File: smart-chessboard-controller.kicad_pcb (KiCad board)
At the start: 4 copper layers, 89.8 x 50.9 mm, 65 parts, among them J1 USB_C_Receptacle_USB2.0, J2 Micro_SD_Card_Det_Hirose_DM3C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, J3 Conn_02x03_Odd_Even, J4 Conn_01x12_MountingPin, J5 NX3224T024, J8 Conn_01x05, J9 Conn_01x05, Q1 S8050, Q2 S8050, SW2 SW_SPST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

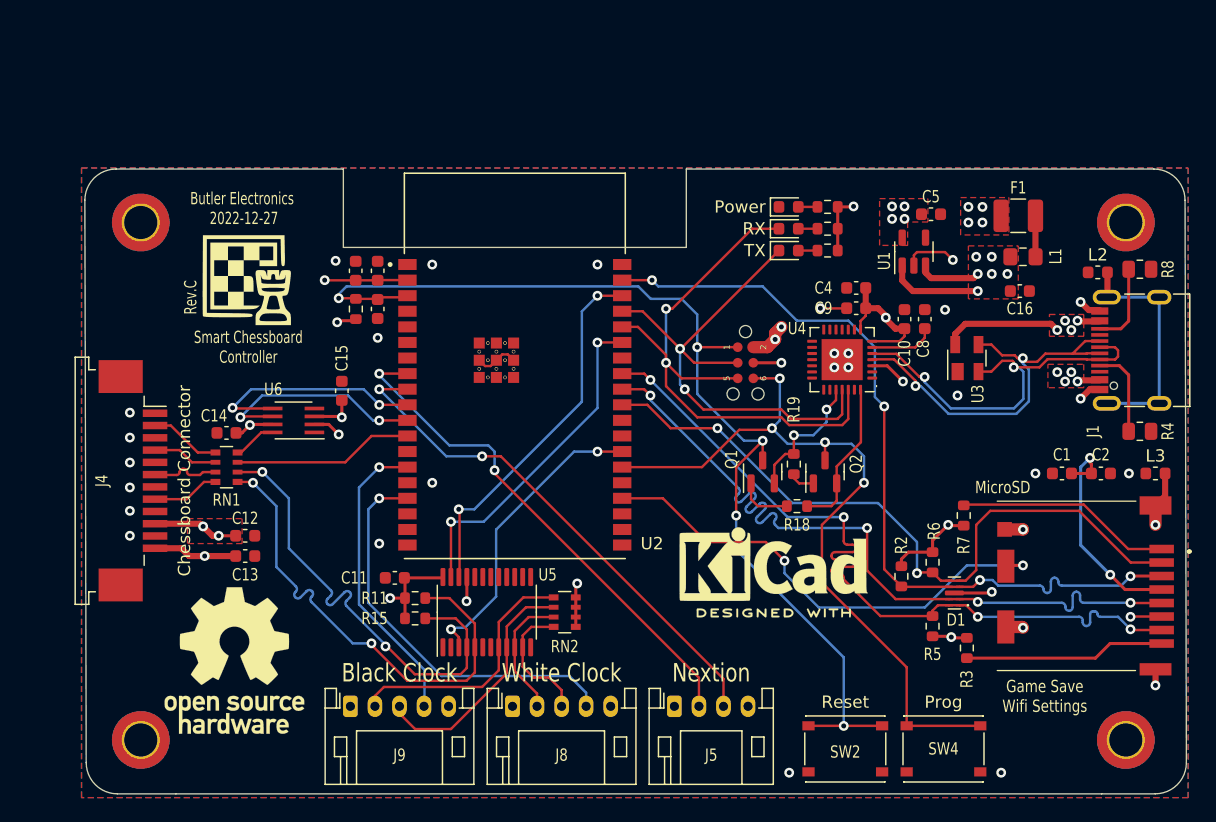
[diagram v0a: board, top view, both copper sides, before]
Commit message: refactor schematic/pcb to add/remove components
- remove ESP programmer Tag Connect interface
- replace set of resistors to resistor array for SD card
- add pull-up resistors for interrupt and bus buffer enable pin
- tune trace length matching for data lines (i2c, ttl and spi)
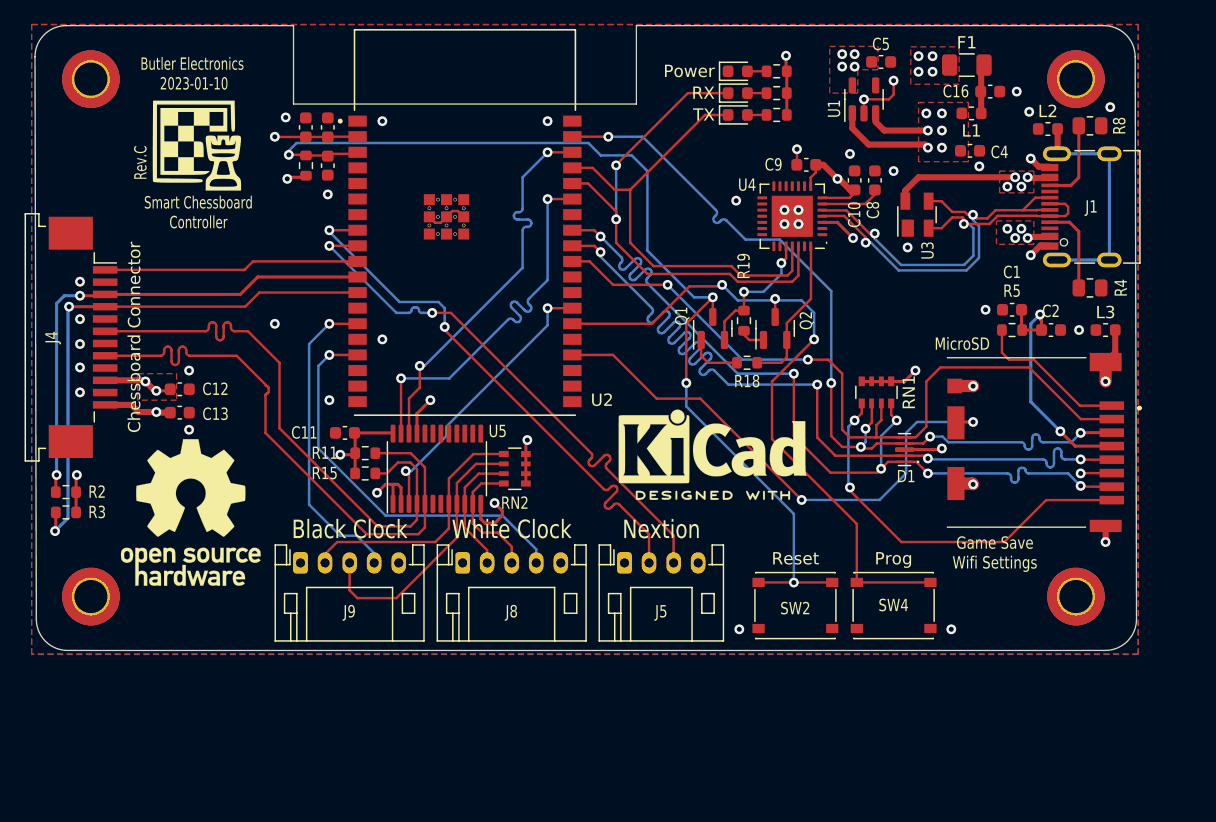
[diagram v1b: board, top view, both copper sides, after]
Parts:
- removed C14, C15: 100nF, Capacitor_SMD:C_0603_1608Metric
- removed J3: Conn_02x03_Odd_Even, Tag_Connect:TC2030-IDC-NL
- removed R6, R7: 47K, Resistor_SMD:R_0603_1608Metric
- removed U6: TXS0102DCT, Package_SO:SSOP-8_2.95x2.8mm_P0.65mm
- F1: value C207047 -> BHFUSE BSMD1206-200-12V; footprint Fuse:Fuse_1210_3225Metric -> Fuse:Fuse_1206_3216Metric
- L1: footprint Inductor_SMD:L_0805_2012Metric_Pad1.15x1.40mm_HandSolder -> Inductor_SMD:L_0603_1608Metric
- R14: value 470 -> 1K
- R2, R3, R5: value 47K -> 10K
- RN1: value 0 -> 10K
- moved R3 74.2 mm to (72.1, 81.3), turned to 180 degrees
- moved R2 68.4 mm to (72.1, 79.6), turned to 180 degrees
- moved RN1 53.3 mm to (138.2, 71.5), turned to 90 degrees
- moved R5 25.0 mm to (149.2, 66.4), turned to 0 degrees
- moved C16 16.4 mm to (147.4, 47.0)
- moved C4 14.5 mm to (145.8, 51.8), turned to 180 degrees
- moved C1 13.9 mm to (149.2, 64.8)
- moved C12 13.1 mm to (81.4, 71.2)
- moved C5 13.1 mm to (138.6, 44.6)
- moved U1 13.1 mm to (137.2, 47.6)
- moved F1 13.0 mm to (145.5, 44.8)
- moved C13 12.8 mm to (81.4, 73.2)
- moved REF** 12.6 mm to (82.3, 81.3)
- moved C11 12.5 mm to (94.9, 74.8)
- moved R11 12.5 mm to (96.5, 76.5)
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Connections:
- C16 pad 2: 5V -> Net-(F1-Pad2)
- J2 pad 8: Net-(J2-Pad8) -> Net-(RN1-Pad1)
- J4 pad 1: GND -> /LED_IC
- J4 pad 2: Net-(J4-Pad2) -> GND
- J4 pad 3: GND -> /~{BUF_EN}
- J4 pad 4: Net-(J4-Pad4) -> /~{IO_INT}
- J4 pad 6: Net-(J4-Pad6) -> ~{SDA_IOMUX}
- J4 pad 8: Net-(J4-Pad8) -> ~{SCL_IOMUX}
- R2 pad 1: /SD_MOSI -> 3V3
- R2 pad 2: 3V3 -> /~{BUF_EN}
- R3 pad 1: Net-(J2-Pad8) -> 3V3
- R3 pad 2: 3V3 -> /~{IO_INT}
- R5 pad 1: /SD_MISO -> Net-(J2-Pad1)
- RN1 pad 1: Net-(J4-Pad2) -> Net-(RN1-Pad1)
- RN1 pad 2: Net-(J4-Pad4) -> /SD_MOSI
- RN1 pad 3: Net-(J4-Pad6) -> /SD_SS
- RN1 pad 4: Net-(J4-Pad8) -> /SD_MISO
- RN1 pad 5: ~{SCL_IOMUX} -> 3V3
- RN1 pad 6: ~{SDA_IOMUX} -> 3V3
- RN1 pad 7: /IO_INT -> 3V3
- RN1 pad 8: /LED_IC_5 -> 3V3
- U2 pad 10: /LED_IC_3 -> /LED_IC
- U2 pad 11: /VLS_EN -> /~{BUF_EN}
- U2 pad 12: /IO_INT -> /~{IO_INT}
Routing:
- net /~{IO_INT}: track 0.00 -> 44.3 mm, vias 0 -> 2
- net /~{BUF_EN}: track 0.00 -> 40.8 mm, vias 0 -> 2
- net Net-(RN1-Pad1): track 0.00 -> 32.1 mm, vias 0 -> 2
- net VBUS: track 58.0 -> 30.4 mm, vias 14 -> 12
- net /LED_IC: track 0.00 -> 20.9 mm
- net /LED_IC_3: track 18.7 -> 0.00 mm, vias 2 -> 0
- net /VLS_EN: track 17.8 -> 0.00 mm, vias 2 -> 0
- net 5V: track 137.2 -> 120.3 mm, vias 10 -> 9
- net Net-(J2-Pad8): track 16.4 -> 0.00 mm
- net 3V3: track 302.3 -> 286.0 mm, vias 15 -> 14
- net /IO_INT: track 14.7 -> 0.00 mm
- net /SD_SCK: track 62.8 -> 71.9 mm
- net ~{SDA_IOMUX}: track 37.7 -> 46.7 mm, vias 2 -> 0
- net ~{SCL_IOMUX}: track 39.5 -> 47.7 mm, vias 2 -> 0
- net /ESP_RX: track 48.5 -> 41.8 mm
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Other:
- board text added: "JLCJLCJLCJLCJLCJLC"

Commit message: update manufacturing files
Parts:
- U2: value ESP32-WROVER-32E -> ESP32-WROVER-E-N8R8
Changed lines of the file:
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@@
   (net 9 "/SD_SS")
   (net 10 "VBUS")
-  (net 11 "Net-(F1-Pad2)")
+  (net 11 "Net-(C16-Pad2)")
   (net 12 "/D_P")
   (net 13 "/D_N")
@@
   (net 38 "unconnected-(U2-Pad5)")
   (net 39 "/~{IO_INT}")
-  (net 40 "Net-(RN1-Pad1)")
+  (net 40 "Net-(J2-Pad8)")
   (net 41 "unconnected-(U2-Pad17)")
   (net 42 "unconnected-(U2-Pad18)")
@@
     (descr "Inductor SMD 0603 (1608 Metric), square (rectangular) end terminal, IPC_7351 nominal, (Body size source: http://www.tortai-tech.com/upload/download/2011102023233369053.pdf), generated with kicad-footprint-generator")
     (tags "inductor")
-    (property "LCSC" "C113018")
+    (property "LCSC" "C62708")
     (property "MFR_PART_NBR" "")
     (property "Sheetfile" "File: smart-chessboard-controller.kicad_sch")
@@
   (footprint "User Custom Footprint:XCVR_ESP32-WROVER-E-N4R8" (layer "F.Cu")
     (at 104.646 57.658)
-    (property "LCSC" " C2973667")
+    (property "LCSC" "C701348")
     (property "MANUFACTURER" "Espressif Systems")
     (property "MAXIMUM_PACKAGE_HEIGHT" "3.45 mm")
@@
       (effects (font (size 1 1) (thickness 0.15)))
     )
-    (fp_text value "ESP32-WROVER-32E" (at 6.24 18.515) (layer "F.Fab")
+    (fp_text value "ESP32-WROVER-E-N8R8" (at 6.24 18.515) (layer "F.Fab")
       (effects (font (size 1 1) (thickness 0.15)))
     )
@@
       (net 6 "/SD_MISO") (pinfunction "DAT0") (pintype "bidirectional"))
     (pad "8" smd rect (at -4.5 6.35 90) (size 0.7 2) (layers "F.Cu" "F.Paste" "F.Mask")
-      (net 40 "Net-(RN1-Pad1)") (pinfunction "DAT1") (pintype "bidirectional"))
+      (net 40 "Net-(J2-Pad8)") (pinfunction "DAT1") (pintype "bidirectional"))
     (pad "9" smd rect (at 1.8 -6.35 90) (size 2.7 1.4) (layers "F.Cu" "F.Paste" "F.Mask")
       (net 17 "/SD_DET") (pinfunction "DET_B") (pintype "passive"))
@@
     (fp_line (start 0.8 0.4) (end -0.8 0.4) (layer "F.Fab") (width 0.1))
     (pad "1" smd roundrect (at -0.7875 0 180) (size 0.875 0.95) (layers "F.Cu" "F.Paste" "F.Mask") (roundrect_rratio 0.25)
-      (net 11 "Net-(F1-Pad2)") (pintype "passive"))
+      (net 11 "Net-(C16-Pad2)") (pintype "passive"))
     (pad "2" smd roundrect (at 0.7875 0 180) (size 0.875 0.95) (layers "F.Cu" "F.Paste" "F.Mask") (roundrect_rratio 0.25)
       (net 4 "5V") (pintype "passive"))
@@
     (fp_line (start -0.8 1.6) (end -0.8 -1.6) (layer "F.Fab") (width 0.1))
     (pad "1" smd rect (at -0.9 -1.2 90) (size 0.8 0.5) (layers "F.Cu" "F.Paste" "F.Mask")
-      (net 40 "Net-(RN1-Pad1)") (pinfunction "R1.1") (pintype "passive"))
+      (net 40 "Net-(J2-Pad8)") (pinfunction "R1.1") (pintype "passive"))
     (pad "2" smd rect (at -0.9 -0.4 90) (size 0.8 0.4) (layers "F.Cu" "F.Paste" "F.Mask")
       (net 8 "/SD_MOSI") (pinfunction "R2.1") (pintype "passive"))
@@
       (net 2 "GND") (pintype "passive"))
     (pad "2" smd roundrect (at 0.775 0 180) (size 0.9 0.95) (layers "F.Cu" "F.Paste" "F.Mask") (roundrect_rratio 0.25)
-      (net 11 "Net-(F1-Pad2)") (pintype "passive"))
+      (net 11 "Net-(C16-Pad2)") (pintype "passive"))
     (model "${KICAD6_3DMODEL_DIR}/Capacitor_SMD.3dshapes/C_0603_1608Metric.wrl"
       (offset (xyz 0 0 0))
@@
       (net 10 "VBUS") (pintype "passive"))
     (pad "2" smd roundrect (at 1.4 0) (size 1.25 1.75) (layers "F.Cu" "F.Paste" "F.Mask") (roundrect_rratio 0.2)
-      (net 11 "Net-(F1-Pad2)") (pintype "passive"))
+      (net 11 "Net-(C16-Pad2)") (pintype "passive"))
     (model "${KICAD6_3DMODEL_DIR}/Fuse.3dshapes/Fuse_1206_3216Metric.wrl"
       (offset (xyz 0 0 0))
@@
     (descr "Inductor SMD 0603 (1608 Metric), square (rectangular) end terminal, IPC_7351 nominal, (Body size source: http://www.tortai-tech.com/upload/download/2011102023233369053.pdf), generated with kicad-footprint-generator")
     (tags "inductor")
-    (property "LCSC" "C113018")
+    (property "LCSC" "C62708")
     (property "MFR_PART_NBR" "")
     (property "Sheetfile" "File: smart-chessboard-controller.kicad_sch")

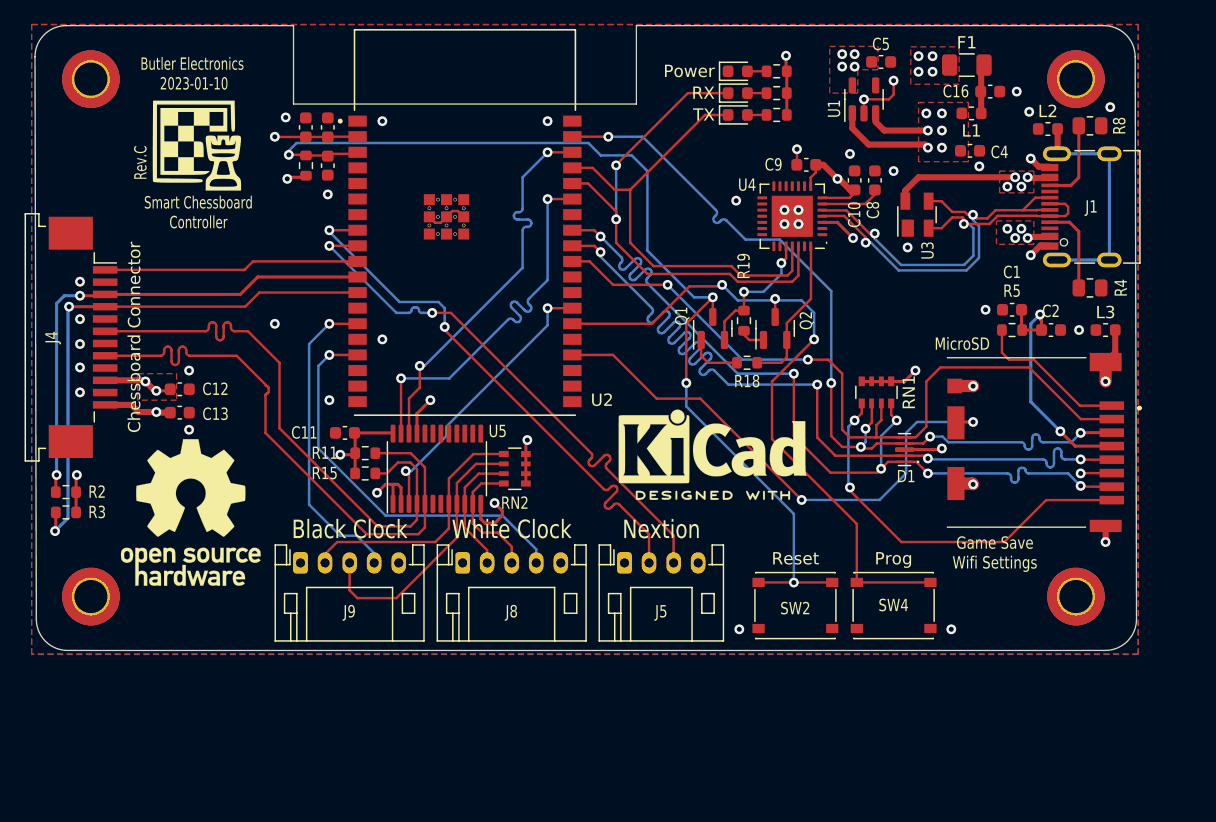
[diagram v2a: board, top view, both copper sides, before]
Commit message: update SD card detect pin assignment
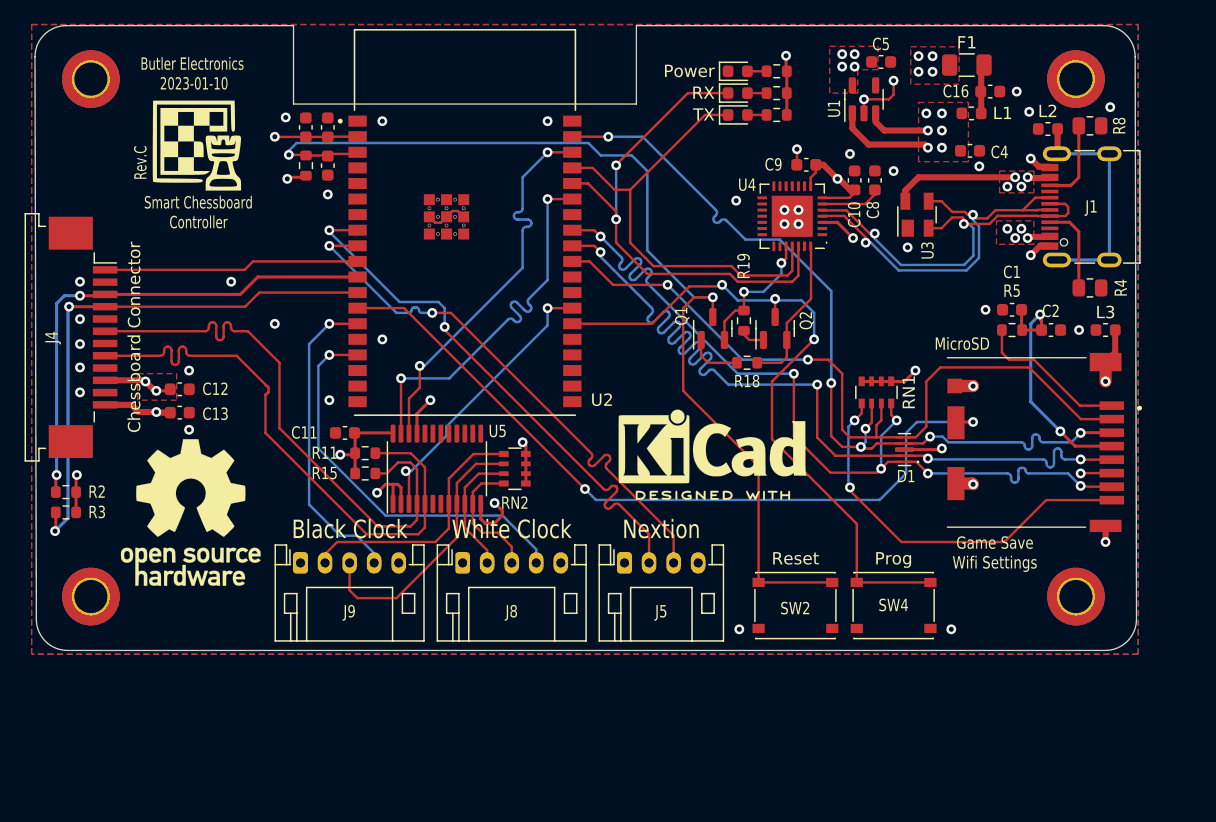
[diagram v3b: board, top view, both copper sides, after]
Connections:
- U2 pad 13: unconnected-(U2-Pad13) -> /SD_DET
- U2 pad 23: /SD_DET -> unconnected-(U2-Pad23)
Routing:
- net /SD_DET: track 43.5 -> 62.6 mm
- net /EN: track 85.3 -> 85.2 mm, vias 4 -> 2
- net GND: vias 41 -> 42

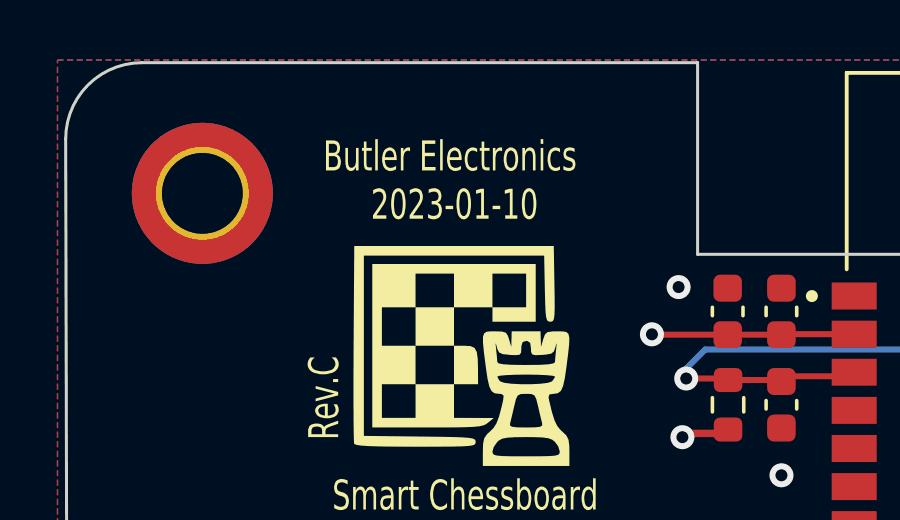
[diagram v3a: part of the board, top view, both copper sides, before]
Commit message: replace USB-C part that was out of stock
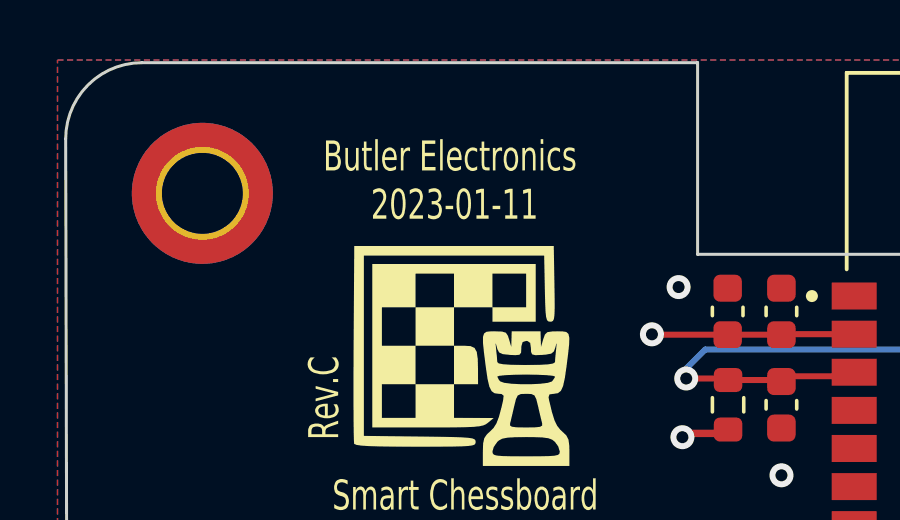
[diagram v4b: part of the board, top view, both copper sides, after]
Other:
- board text added: "JLCJLCJLCJLC"
- board text removed: "JLCJLCJLCJLCJLCJLC"
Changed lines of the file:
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@@
 (kicad_pcb (version 20211014) (generator pcbnew)
   (general
-    (thickness 1.6)
+    (thickness 1.6062)
   )
   (paper "A5")
   (title_block
     (title "Smart Chessboard Controller")
-    (date "2023-01-10")
+    (date "2023-01-11")
     (rev "C")
     (company "Butler Electronics")
@@
       (layer "F.Mask" (type "Top Solder Mask") (color "Black") (thickness 0.01))
       (layer "F.Cu" (type "copper") (thickness 0.035))
-      (layer "dielectric 1" (type "core") (thickness 0.48) (material "FR4") (epsilon_r 4.5) (loss_tangent 0.02))
-      (layer "In1.Cu" (type "copper") (thickness 0.035))
-      (layer "dielectric 2" (type "prepreg") (thickness 0.48) (material "FR4") (epsilon_r 4.5) (loss_tangent 0.02))
-      (layer "In2.Cu" (type "copper") (thickness 0.035))
-      (layer "dielectric 3" (type "core") (thickness 0.48) (material "FR4") (epsilon_r 4.5) (loss_tangent 0.02))
+      (layer "dielectric 1" (type "prepreg") (thickness 0.2104) (material "FR4") (epsilon_r 4.5) (loss_tangent 0.02))
+      (layer "In1.Cu" (type "copper") (thickness 0.0152))
+      (layer "dielectric 2" (type "core") (thickness 1.065) (material "FR4") (epsilon_r 4.5) (loss_tangent 0.02))
+      (layer "In2.Cu" (type "copper") (thickness 0.0152))
+      (layer "dielectric 3" (type "prepreg") (thickness 0.2104) (material "FR4") (epsilon_r 4.5) (loss_tangent 0.02))
       (layer "B.Cu" (type "copper") (thickness 0.035))
       (layer "B.Mask" (type "Bottom Solder Mask") (color "Black") (thickness 0.01))
@@
     (descr "USB TYPE C, USB 2.0, SMT, https://datasheet.lcsc.com/lcsc/2103051833_Jing-Extension-of-the-Electronic-Co--918-418K2023S40001_C167321.pdf")
     (tags "USB C Type-C Receptacle SMD USB 2.0")
-    (property "LCSC" "C167321")
+    (property "LCSC" "C2982555")
     (property "Sheetfile" "File: smart-chessboard-controller.kicad_sch")
     (property "Sheetname" "")
@@
   (gr_line (start 90.676 41.618) (end 72.152051 41.618) (layer "Edge.Cuts") (width 0.1))
   (gr_line (start 118.616 41.618) (end 156.716 41.618) (layer "Edge.Cuts") (width 0.1))
-  (gr_text "JLCJLCJLCJLCJLCJLC" (at 84.328 67.31 90) (layer "B.SilkS")
+  (gr_text "JLCJLCJLCJLC" (at 84.328 67.31 90) (layer "B.SilkS")
     (effects (font (size 1.2 1) (thickness 0.153)) (justify mirror))
   )
